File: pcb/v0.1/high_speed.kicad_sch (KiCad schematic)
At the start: 22 parts, among them J4 TYPE_C_Receptacle, J5 TYPE_C_Receptacle, J6 22s_disp_connector, J7 ComputeModule5-CM5_connector, U2 Nexperia PUSB3FR4Z, U3 Nexperia PUSB3FR4Z, U8 AP22653W6-7

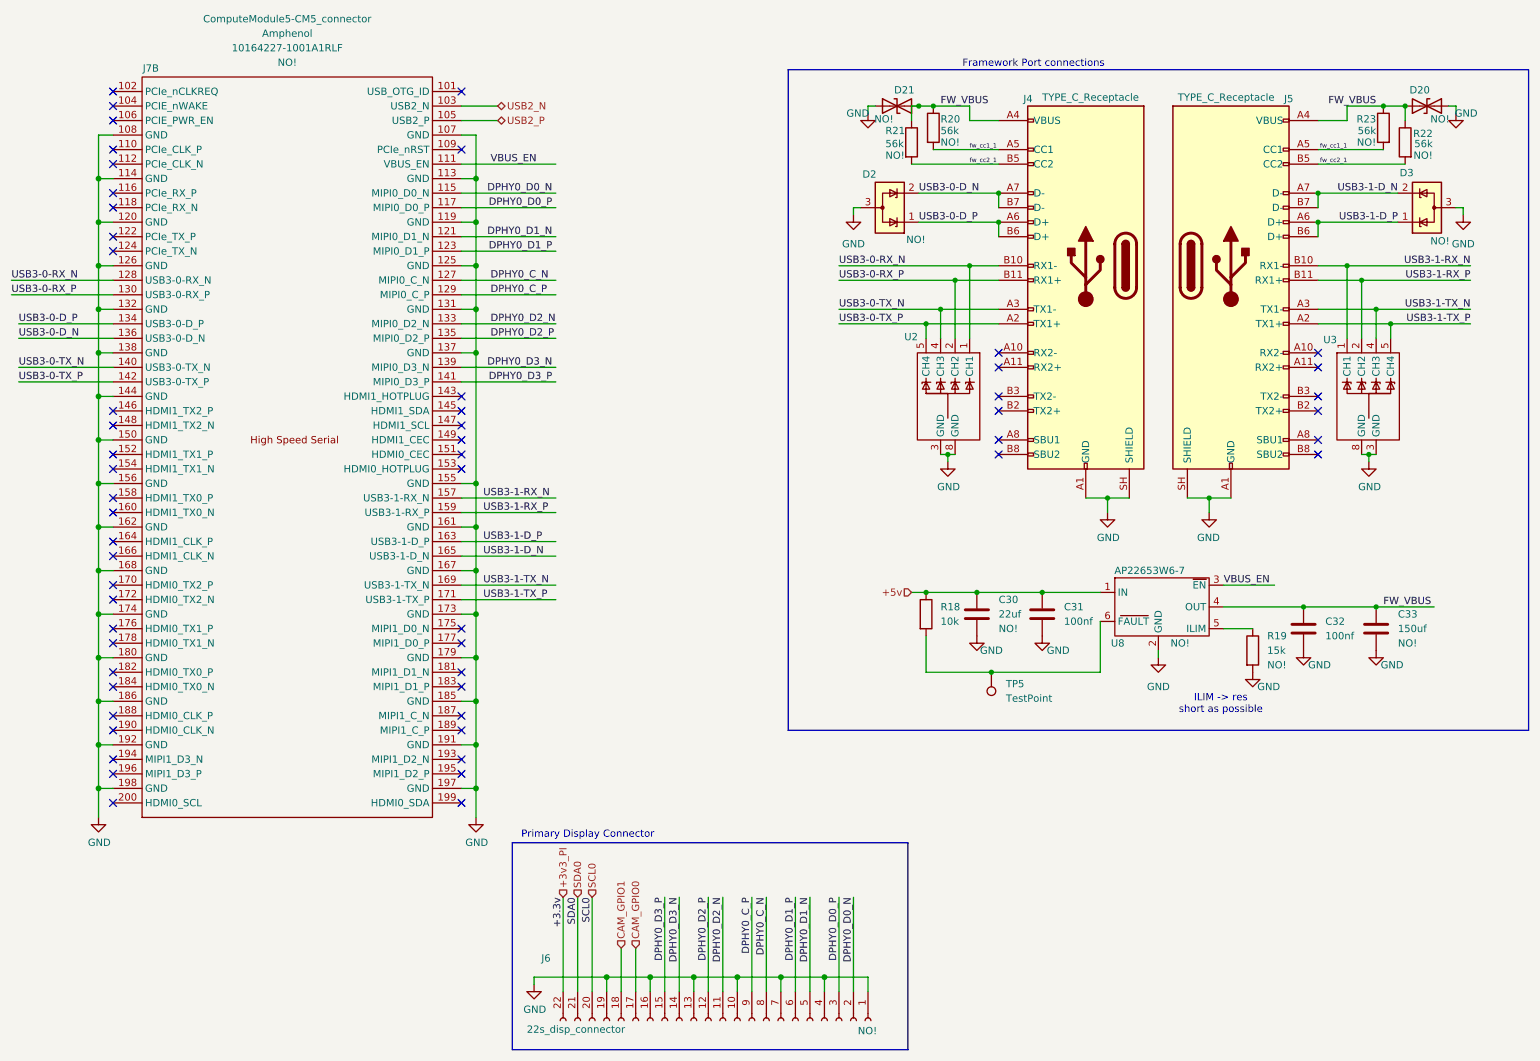
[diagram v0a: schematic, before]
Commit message: Make the ERC happy
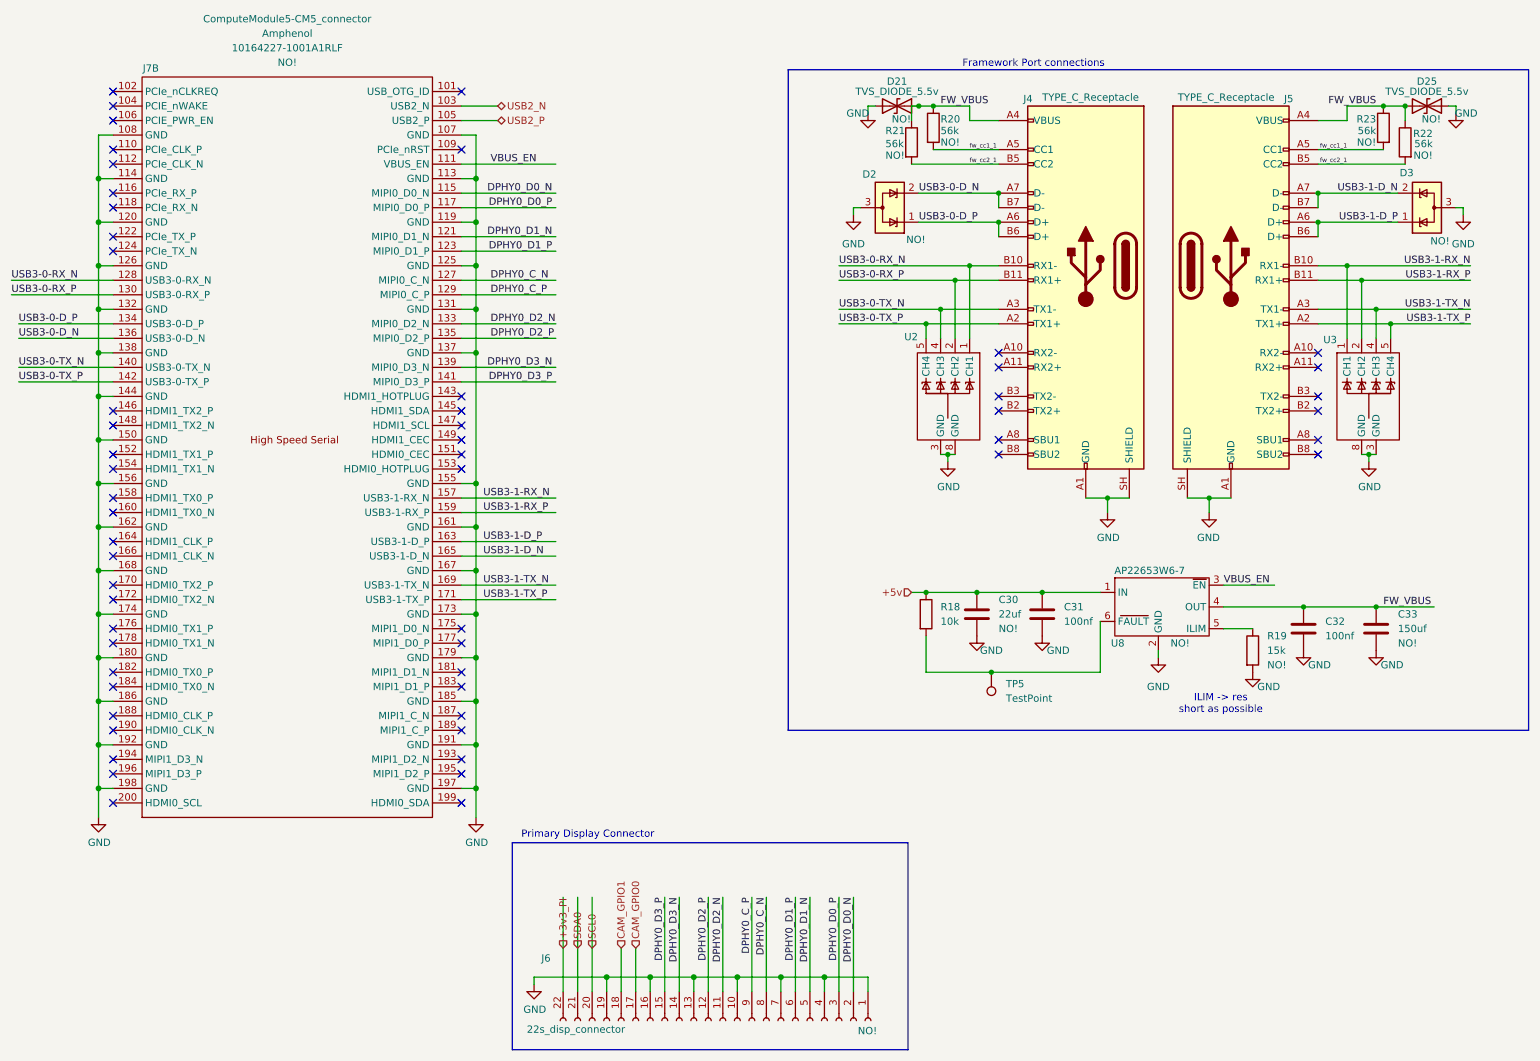
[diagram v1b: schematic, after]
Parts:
- removed D20, D21: TVS_DIODE_7.1VC, Diode_SMD:D_SOD-882, symbol TH-1-CC:TVS_DIODE_7.1VC
- added D21, D25: TVS_DIODE_5.5v, Diode_SMD:D_SOD-882, symbol TH-1-CC:TVS_DIODE_5.5v
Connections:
- net FW_VBUS: now also D21.2 (A2), D25.1 (A1)
- net GND: now also D21.1 (A1), D25.2 (A2)

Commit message: Small corrections
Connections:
- net FW_VBUS: now also U8.6 (OUT); no longer R21.1, U8.4 (OUT)
- net at R18.2, TP5.1: now also U8.4 (FAULT); no longer U8.6 (FAULT)
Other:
- moved on the sheet: D21
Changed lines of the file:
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@@
 	)
 	(junction
-		(at 175.26 30.48)
-		(diameter 0)
-		(color 0 0 0 0)
-	)
-	(junction
 		(at 97.79 73.66)
 		(diameter 1.016)
@@
 	(wire
 		(pts
-			(xy 173.99 30.48) (xy 175.26 30.48)
-		)
-		(stroke
-			(width 0)
-			(type default)
-		)
-	)
-	(wire
-		(pts
 			(xy 95.25 50.8) (xy 97.79 50.8)
 		)
@@
 	(wire
 		(pts
+			(xy 171.45 30.48) (xy 177.8 30.48)
+		)
+		(stroke
+			(width 0)
+			(type default)
+		)
+	)
+	(wire
+		(pts
 			(xy 180.34 91.44) (xy 180.34 92.71)
 		)
@@
 	(wire
 		(pts
-			(xy 113.03 185.42) (xy 113.03 168.91)
+			(xy 113.03 185.42) (xy 113.03 177.8)
 		)
 		(stroke
@@
 	(wire
 		(pts
-			(xy 115.57 185.42) (xy 115.57 168.91)
+			(xy 115.57 185.42) (xy 115.57 177.8)
 		)
 		(stroke
@@
 	(wire
 		(pts
-			(xy 166.37 30.48) (xy 166.37 31.75)
+			(xy 162.56 30.48) (xy 162.56 31.75)
 		)
 		(stroke
@@
 	(wire
 		(pts
-			(xy 175.26 30.48) (xy 177.8 30.48)
-		)
-		(stroke
-			(width 0)
-			(type default)
-		)
-	)
-	(wire
-		(pts
-			(xy 167.64 30.48) (xy 166.37 30.48)
+			(xy 163.83 30.48) (xy 162.56 30.48)
 		)
 		(stroke
@@
 	(wire
 		(pts
-			(xy 118.11 185.42) (xy 118.11 168.91)
+			(xy 118.11 185.42) (xy 118.11 177.8)
 		)
 		(stroke
@@
 	(symbol
 		(lib_id "TH-1-CC:TVS_DIODE_5.5v")
-		(at 171.45 30.48 0)
+		(at 167.64 30.48 0)
 		(unit 1)
 		(body_style 1)
@@
 		(dnp no)
 		(property "Reference" "D21"
-			(at 171.45 26.162 0)
+			(at 167.64 26.162 0)
 			(show_name no)
 			(do_not_autoplace no)
@@
 		)
 		(property "Value" "TVS_DIODE_5.5v"
-			(at 171.45 27.94 0)
+			(at 167.64 27.94 0)
 			(show_name no)
 			(do_not_autoplace no)
@@
 		)
 		(property "Footprint" "Diode_SMD:D_SOD-882"
-			(at 171.45 35.56 0)
+			(at 167.64 35.56 0)
 			(hide yes)
 			(show_name no)
@@
 		)
 		(property "Datasheet" "https://www.lcsc.com/datasheet/C553450.pdf?spm=wm.sxq.inf.ggs&lcsc_vid=QAILXlUCRldfUlcDQgANV1IDE1JYXwJWRANcAwFRRgAxVlNeRVdYVVNVQFFWVDsOAxUeFF5JWBYZEEoKFBINSQcJGk4NBhADEA4cHktRR1NADxALGw%3D%3D"
-			(at 171.45 30.48 0)
+			(at 167.64 30.48 0)
 			(hide yes)
 			(show_name no)
@@
 		)
 		(property "Description" "TVS DIODE 5.5VWM 7.1VC DFN1006-2(SOD-882)"
-			(at 171.45 30.48 0)
+			(at 167.64 30.48 0)
 			(hide yes)
 			(show_name no)
@@
 		)
 		(property "Manufacturer" "Nexperia"
-			(at 171.45 30.48 0)
+			(at 167.64 30.48 0)
 			(hide yes)
 			(show_name no)
@@
 		)
 		(property "Mfr. Part no." "PTVS5V5D1BLYL"
-			(at 171.45 30.48 0)
+			(at 167.64 30.48 0)
 			(hide yes)
 			(show_name no)
@@
 		)
 		(property "Distributor DigiKey" "https://www.lcsc.com/product-detail/C553450.html?lcsc_vid=QAILXlUCRldfUlcDQgANV1IDE1JYXwJWRANcAwFRRgAxVlNeRVdYVVNVQFFWVDsOAxUeFF5JWBYZEEoKFBINSQcJGk4NBhADEA4cHktRR1NADxALGw%3D%3D"
-			(at 171.45 30.48 0)
+			(at 167.64 30.48 0)
 			(hide yes)
 			(show_name no)
@@
 		)
 		(property "LCSC Part no." "C553450"
-			(at 171.45 30.48 0)
+			(at 167.64 30.48 0)
 			(hide yes)
 			(show_name no)
@@
 		)
 		(property "Stock" "NO!"
-			(at 172.212 32.766 0)
+			(at 168.402 32.766 0)
 			(show_name no)
 			(do_not_autoplace no)
@@
 	(symbol
 		(lib_id "power:GND")
-		(at 166.37 31.75 0)
+		(at 162.56 31.75 0)
 		(mirror y)
 		(unit 1)
@@
 		(dnp no)
 		(property "Reference" "#PWR069"
-			(at 166.37 38.1 0)
+			(at 162.56 38.1 0)
 			(hide yes)
 			(show_name no)
@@
 		)
 		(property "Value" "GND"
-			(at 164.592 31.75 0)
+			(at 160.782 31.75 0)
 			(show_name no)
 			(do_not_autoplace no)
@@
 		)
 		(property "Footprint" ""
-			(at 166.37 31.75 0)
+			(at 162.56 31.75 0)
 			(hide yes)
 			(show_name no)
@@
 		)
 		(property "Datasheet" ""
-			(at 166.37 31.75 0)
+			(at 162.56 31.75 0)
 			(hide yes)
 			(show_name no)
@@
 		)
 		(property "Description" "Power symbol creates a global label with name \"GND\" , ground"
-			(at 166.37 31.75 0)
+			(at 162.56 31.75 0)
 			(hide yes)
 			(show_name no)
